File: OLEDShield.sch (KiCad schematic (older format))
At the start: 12 parts, among them P1 CONN_5X2, P2 CONN_5X2

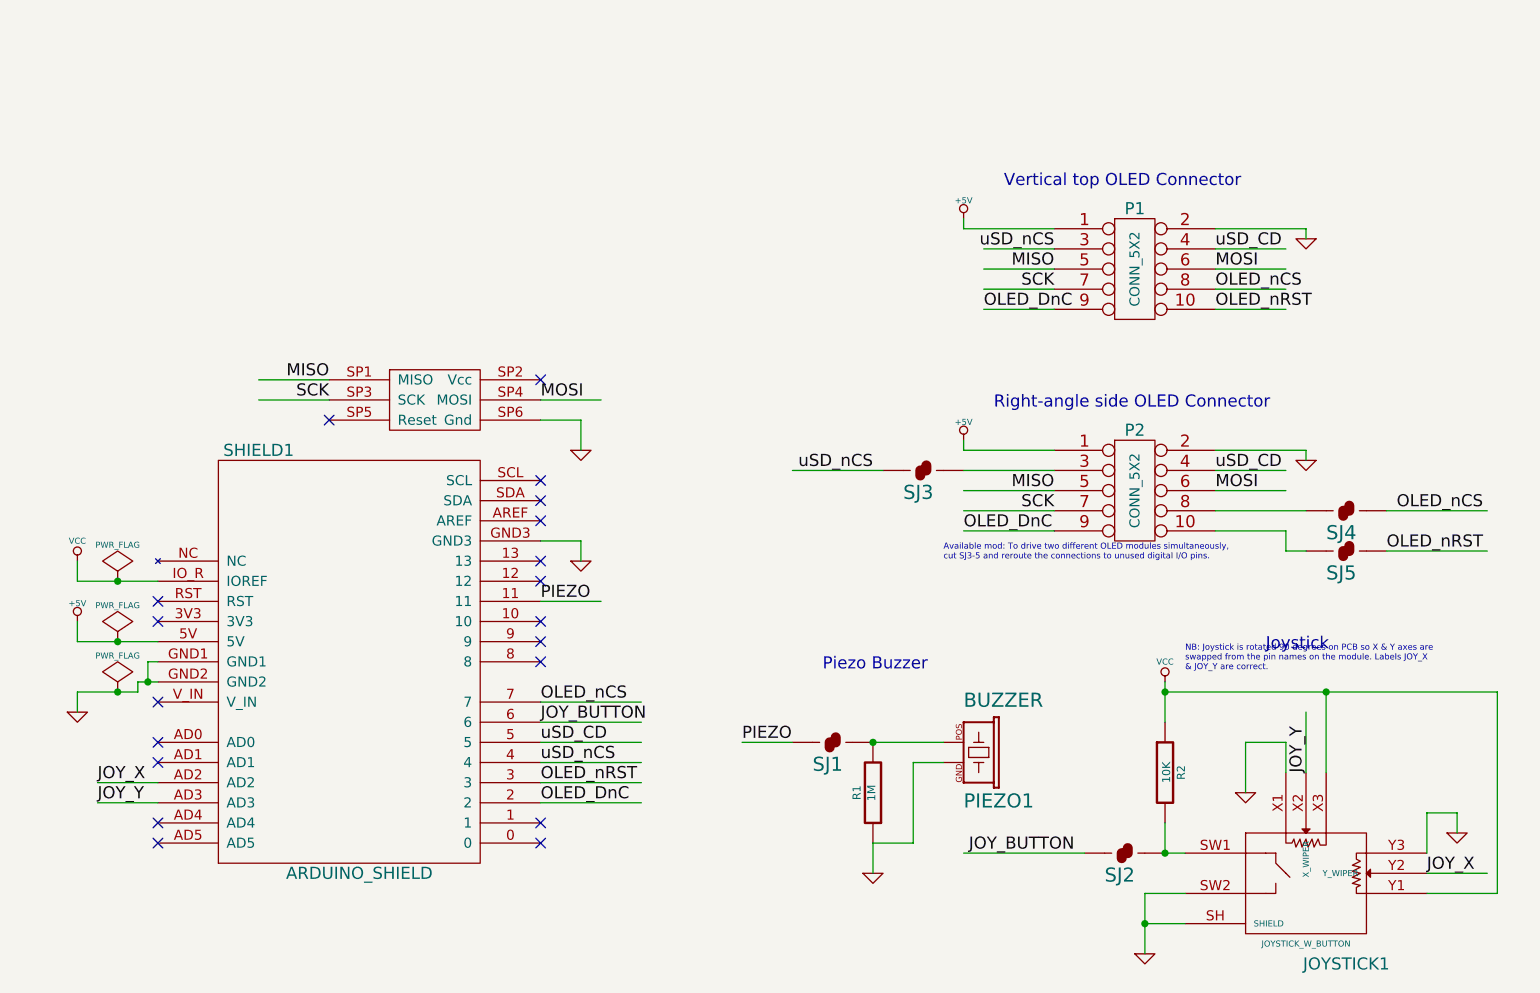
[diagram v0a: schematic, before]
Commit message: Board largely done, no silkscreen labels yet
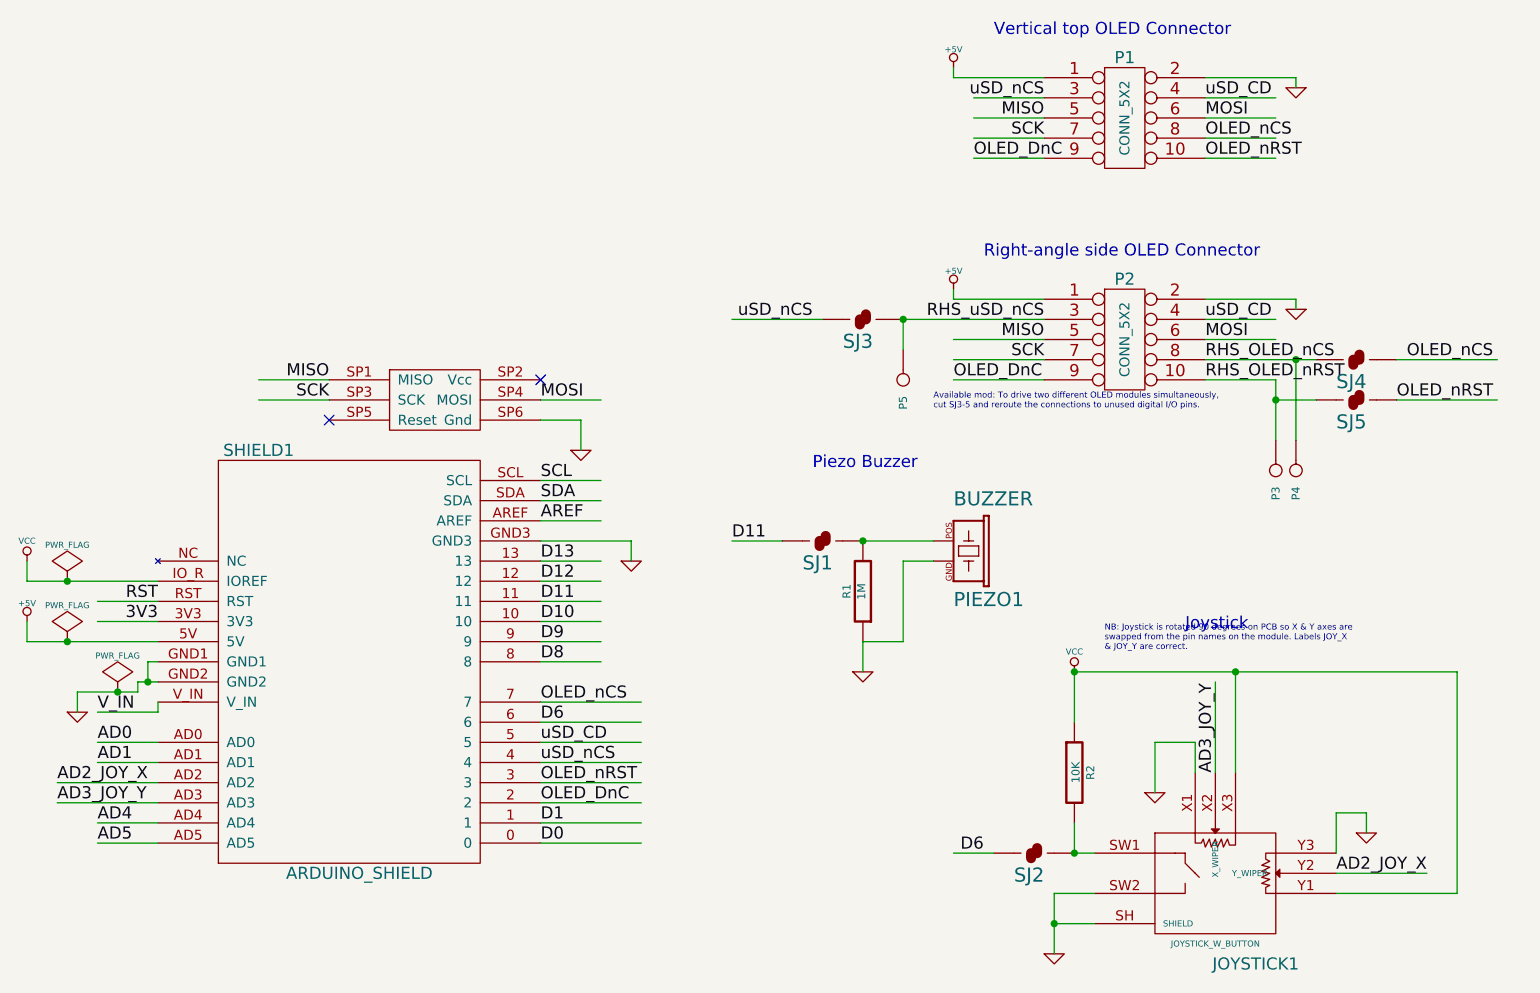
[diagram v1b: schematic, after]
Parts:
- added P3, P4, P5: CONN_1, ~, symbol CONN_1
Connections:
- net labels added: 3V3, AD0, AD1, AD2_JOY_X, AD3_JOY_Y, AD4, AD5, AREF, D0, D1, D10, D11, D12, D13, D6, D8, D9, RHS_OLED_nCS, RHS_OLED_nRST, RHS_uSD_nCS, RST, SCL, SDA, V_IN
- net labels removed: JOY_BUTTON, JOY_X, JOY_Y, PIEZO
- wire segments 80 -> 100
- no-connect marks 19 -> 2
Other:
- moved on the sheet: JOYSTICK1, P1, P2, PIEZO1, R1, R2, SJ1, SJ2, SJ3, SJ4, SJ5
